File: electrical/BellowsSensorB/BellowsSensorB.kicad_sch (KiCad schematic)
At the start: 5 parts, among them J1 I2C, U1 CPS610DSD010DH01

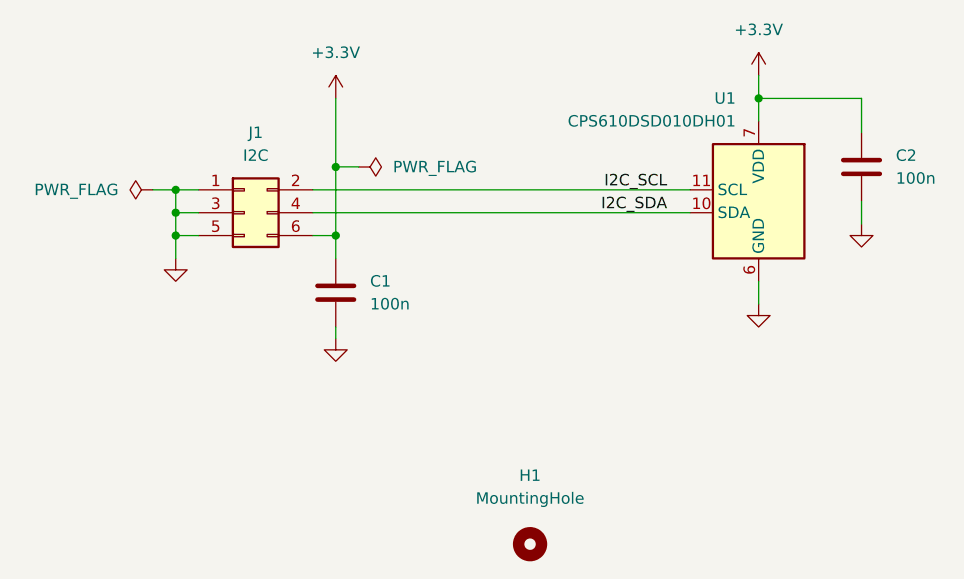
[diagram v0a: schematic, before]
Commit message: Switch pressure sensor for BellowsSensorB
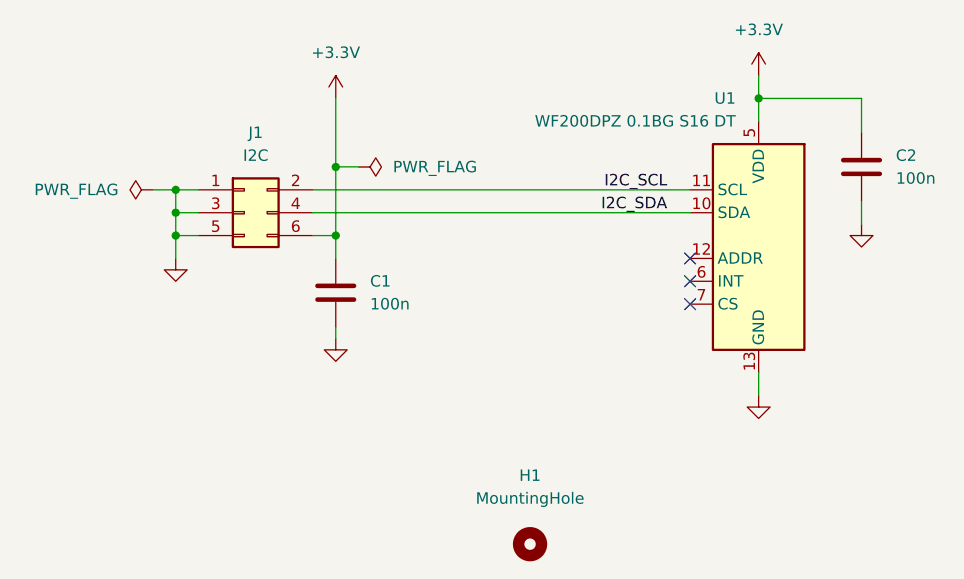
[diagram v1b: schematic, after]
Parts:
- removed U1: CPS610DSD010DH01, Package_SO:SOIC-16W_7.5x10.3mm_P1.27mm, symbol MidiConcertina:Consensic_CPS610x
- added U1: WF200DPZ 0.1BG S16 DT, Package_SO:SOIC-16W_7.5x10.3mm_P1.27mm, symbol MidiConcertina:WF_WF200Dx
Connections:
- net +3.3V: now also U1.5 (VDD)
- net GND: now also U1.13 (GND)
- net I2C_SCL: now also U1.11 (SCL)
- net I2C_SDA: now also U1.10 (SDA)
- no-connect marks 0 -> 3
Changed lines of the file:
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@@
 		(color 0 0 0 0)
 	)
+	(no_connect
+		(at 151.13 87.63)
+	)
+	(no_connect
+		(at 151.13 90.17)
+	)
+	(no_connect
+		(at 151.13 85.09)
+	)
 	(wire
 		(pts
@@
 	(wire
 		(pts
-			(xy 158.75 90.17) (xy 158.75 87.63)
+			(xy 158.75 100.33) (xy 158.75 97.79)
 		)
 		(stroke
@@
 	)
 	(symbol
+		(lib_id "MidiConcertina:WF_WF200Dx")
+		(at 158.75 82.55 0)
+		(mirror y)
+		(unit 1)
+		(exclude_from_sim no)
+		(in_bom yes)
+		(on_board yes)
+		(dnp no)
+		(property "Reference" "U1"
+			(at 156.21 67.31 0)
+			(effects
+				(font
+					(size 1.27 1.27)
+				)
+				(justify left)
+			)
+		)
+		(property "Value" "WF200DPZ 0.1BG S16 DT"
+			(at 156.21 69.85 0)
+			(effects
+				(font
+					(size 1.27 1.27)
+				)
+				(justify left)
+			)
+		)
+		(property "Footprint" "Package_SO:SOIC-16W_7.5x10.3mm_P1.27mm"
+			(at 158.75 82.55 0)
+			(effects
+				(font
+					(size 1.27 1.27)
+				)
+				(hide yes)
+			)
+		)
+		(property "Datasheet" "https://jlcpcb.com/api/file/downloadByFileSystemAccessId/8603406260650205184"
+			(at 158.75 82.55 0)
+			(effects
+				(font
+					(size 1.27 1.27)
+				)
+				(hide yes)
+			)
+		)
+		(property "Description" "Pressure Sensor ±10kPa Differential Male - 2.2mm Tube, Dual Ports, ROHS"
+			(at 158.75 82.55 0)
+			(effects
+				(font
+					(size 1.27 1.27)
+				)
+				(hide yes)
+			)
+		)
+		(property "LCSC" "C3001195"
+			(at 158.75 82.55 0)
+			(effects
+				(font
+					(size 1.27 1.27)
+				)
+				(hide yes)
+			)
+		)
+		(property "Part" "WF WF200DPZ 0.1BG S16 DT"
+			(at 158.75 82.55 0)
+			(effects
+				(font
+					(size 1.27 1.27)
+				)
+				(hide yes)
+			)
+		)
+		(pin "7"
+		)
+		(pin "15"
+		)
+		(pin "14"
+		)
+		(pin "16"
+		)
+		(pin "1"
+		)
+		(pin "9"
+		)
+		(pin "2"
+		)
+		(pin "4"
+		)
+		(pin "3"
+		)
+		(pin "8"
+		)
+		(pin "12"
+		)
+		(pin "13"
+		)
+		(pin "10"
+		)
+		(pin "11"
+		)
+		(pin "6"
+		)
+		(pin "5"
+		)
+		(instances
+			(project ""
+				(path "/ceae7089-9cb4-4950-bb64-2f75302207fd"
+					(reference "U1")
+					(unit 1)
+				)
+			)
+		)
+	)
+	(symbol
 		(lib_id "power:GND")
-		(at 158.75 90.17 0)
+		(at 158.75 100.33 0)
 		(mirror y)
 		(unit 1)
@@
 		(fields_autoplaced yes)
 		(property "Reference" "#PWR05"
-			(at 158.75 96.52 0)
+			(at 158.75 106.68 0)
 			(effects
 				(font
@@
 		)
 		(property "Value" "GND"
-			(at 158.75 95.25 0)
+			(at 158.75 105.41 0)
 			(effects
 				(font
@@
 		)
 		(property "Footprint" ""
-			(at 158.75 90.17 0)
+			(at 158.75 100.33 0)
 			(effects
 				(font
@@
 		)
 		(property "Datasheet" ""
-			(at 158.75 90.17 0)
+			(at 158.75 100.33 0)
 			(effects
 				(font
@@
 		)
 		(property "Description" "Power symbol creates a global label with name \"GND\" , ground"
-			(at 158.75 90.17 0)
+			(at 158.75 100.33 0)
 			(effects
 				(font
@@
 					(unit 1)
 				)
-			)
-		)
-	)
-	(symbol
-		(lib_id "MidiConcertina:Consensic_CPS610x")
-		(at 158.75 80.01 0)
-		(mirror y)
-		(unit 1)
-		(exclude_from_sim no)
-		(in_bom yes)
-		(on_board yes)
-		(dnp no)
-		(property "Reference" "U1"
-			(at 156.21 67.31 0)
-			(effects
-				(font
-					(size 1.27 1.27)
-				)
-				(justify left)
-			)
-		)
-		(property "Value" "CPS610DSD010DH01"
-			(at 156.21 69.85 0)
-			(effects
-				(font
-					(size 1.27 1.27)
-				)
-				(justify left)
-			)
-		)
-		(property "Footprint" "Package_SO:SOIC-16W_7.5x10.3mm_P1.27mm"
-			(at 158.75 80.01 0)
-			(effects
-				(font
-					(size 1.27 1.27)
-				)
-				(hide yes)
-			)
-		)
-		(property "Datasheet" "https://jlcpcb.com/api/file/downloadByFileSystemAccessId/8603406260650205184"
-			(at 158.75 80.01 0)
-			(effects
-				(font
-					(size 1.27 1.27)
-				)
-				(hide yes)
-			)
-		)
-		(property "Description" "Pressure Sensor ±10kPa Differential Male - 2.2mm Tube, Dual Ports, ROHS"
-			(at 158.75 80.01 0)
-			(effects
-				(font
-					(size 1.27 1.27)
-				)
-				(hide yes)
-			)
-		)
-		(property "LCSC" "C28646450"
-			(at 158.75 80.01 0)
-			(effects
-				(font
-					(size 1.27 1.27)
-				)
-				(hide yes)
-			)
-		)
-		(property "Part" "Consensic CPS610DSD010DH01"
-			(at 158.75 80.01 0)
-			(effects
-				(font
-					(size 1.27 1.27)
-				)
-				(hide yes)
-			)
-		)
-		(pin "14"
-		)
-		(pin "15"
-		)
-		(pin "16"
-		)
-		(pin "2"
-		)
-		(pin "3"
-		)
-		(pin "4"
-		)
-		(pin "5"
-		)
-		(pin "8"
-		)
-		(pin "9"
-		)
-		(pin "7"
-		)
-		(pin "12"
-		)
-		(pin "13"
-		)
-		(pin "6"
-		)
-		(pin "11"
-		)
-		(pin "10"
-		)
-		(pin "1"
-		)
-		(instances
-			(project ""
-				(path "/ceae7089-9cb4-4950-bb64-2f75302207fd"
-					(reference "U1")
-					(unit 1)
-				)

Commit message: Update bellows sensor labels
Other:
- title: MIDI Bellows Sensor -> MIDI Bellows Sensor B
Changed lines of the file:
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@@
 	(paper "USLetter")
 	(title_block
-		(title "MIDI Bellows Sensor")
+		(title "MIDI Bellows Sensor B")
 		(date "2026-01-19")
 		(rev "1")
